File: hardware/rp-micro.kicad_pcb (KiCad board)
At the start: 2 copper layers, 17.8 x 33 mm, 46 parts, among them J1 USB_C_Receptacle_USB2.0, J2 Conn_01x12, J3 Conn_01x12, J4 Conn_01x05, SW1 BOOT, SW2 RESET, U1 RT9013-33GB, U2 W25Q16JVUXIQ, U3 RP2040, Y1 12MHz

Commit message: Update
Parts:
- removed the C1 at (144.9, 75.9)
- removed the C4 at (137.2, 66.3)
- removed the R1 at (142.6, 72.1)
- removed the R10 at (143.6, 84.6)
- removed the R6 at (141.1, 72.1)
- removed the R9 at (143.6, 85.6)
- added C15: 0.1uF, Capacitor_SMD:C_0402_1005Metric, F.Cu at (144.9, 75.9)
- added R5: 27, Resistor_SMD:R_0402_1005Metric, F.Cu at (141.1, 72.1)
- added TP2: TestPoint, TestPoint:TestPoint_Pad_D1.0mm, B.Cu at (140.7, 85.0)
- added TP3: TestPoint, TestPoint:TestPoint_Pad_D1.0mm, B.Cu at (138.7, 85.0)
- C16: renamed from C17; value 2.2uF -> 1uF
- C4: renamed from C6; value 15pF -> 20pF
- C5: renamed from C7; value 15pF -> 20pF
- C8: renamed from C10; value 2.2uF -> 1uF
- Y1: footprint Crystal:Crystal_SMD_2520-4Pin_2.5x2.0mm -> Crystal:Crystal_SMD_3225-4Pin_3.2x2.5mm
- moved kibuzzard-6360A6AE 5.50 mm to (137.7, 80.8)
- moved C4 3.94 mm to (134.0, 86.6)
- moved C13 2.54 mm to (140.1, 74.0)
- moved C16 2.54 mm to (142.6, 74.0)
- moved C10 2.33 mm to (141.7, 86.4), turned to 0 degrees
- moved C5 1.94 mm to (139.8, 86.4)
- moved C3 1.52 mm to (136.7, 66.3)
- moved R8 1.40 mm to (139.3, 84.8), turned to 90 degrees
- moved Y1 1.30 mm to (136.7, 85.9), turned to 180 degrees
- moved C6 1.15 mm to (141.7, 85.3), turned to 0 degrees
- moved R9 1.15 mm to (143.8, 85.5), turned to 90 degrees
- renumbered C2 to C1, C12 to C10, C13 to C11, C14 to C12, C15 to C13, C16 to C14, C3 to C2, C5 to C3, C8 to C6, C9 to C7, C11 to C9, R2 to R1, R13 to R10, R3 to R2, R5 to R3, R7 to R6, R8 to R7, R11 to R8, R12 to R9
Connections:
- net 16_SDA renamed 16
- net 17_SCL renamed 17
- J1 pad A6: Net-(J1-PadA6) -> USB_D+
- J1 pad A7: Net-(J1-PadA7) -> USB_D-
- J1 pad B6: Net-(J1-PadA6) -> USB_D+
- J1 pad B7: Net-(J1-PadA7) -> USB_D-
- J1 pad S1: unconnected-(J1-PadS1) -> GND
- J4 pad 1: SWCLK -> 10
- J4 pad 2: SWDIO -> 11
- J4 pad 3: GND -> 12
- R4 pad 1: Net-(J1-PadA7) -> USB_D+
- R4 pad 2: USB_D- -> Net-(R4-Pad2)
- U3 pad 13: unconnected-(U3-Pad13) -> 10
- U3 pad 14: unconnected-(U3-Pad14) -> 11
- U3 pad 15: unconnected-(U3-Pad15) -> 12
- U3 pad 43: Net-(C1-Pad1) -> +3V3
- U3 pad 46: USB_D+ -> Net-(R5-Pad2)
- U3 pad 47: USB_D- -> Net-(R4-Pad2)
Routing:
- net Net-(J1-PadA6): track 11.6 -> 0.00 mm
- net Net-(J1-PadA7): track 10.9 -> 0.00 mm, vias 2 -> 0
- net 11: track 0.00 -> 9.50 mm, vias 0 -> 1
- net GND: track 66.3 -> 57.2 mm, vias 35 -> 27
- net 10: track 0.00 -> 8.71 mm, vias 0 -> 1
- net +3V3: track 76.7 -> 68.9 mm, vias 11 -> 8
- net 12: track 0.00 -> 7.39 mm, vias 0 -> 1
- net USB_D+: track 3.61 -> 10.9 mm
- net USB_D-: track 3.82 -> 10.9 mm, vias 0 -> 2
- net Net-(C1-Pad1): track 6.17 -> 0.00 mm
- net Net-(R4-Pad2): track 0.00 -> 3.82 mm
- net Net-(R5-Pad2): track 0.00 -> 3.61 mm
- net Net-(C4-Pad2): track 6.19 -> 7.76 mm
- net SWDIO: track 8.85 -> 10.0 mm, vias 0 -> 1
- net 16: track 9.02 -> 10.0 mm
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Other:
- board text added: "10"
- board text added: "11"
- board text added: "12"
- board text removed: "SWC"
- board text removed: "SWD"

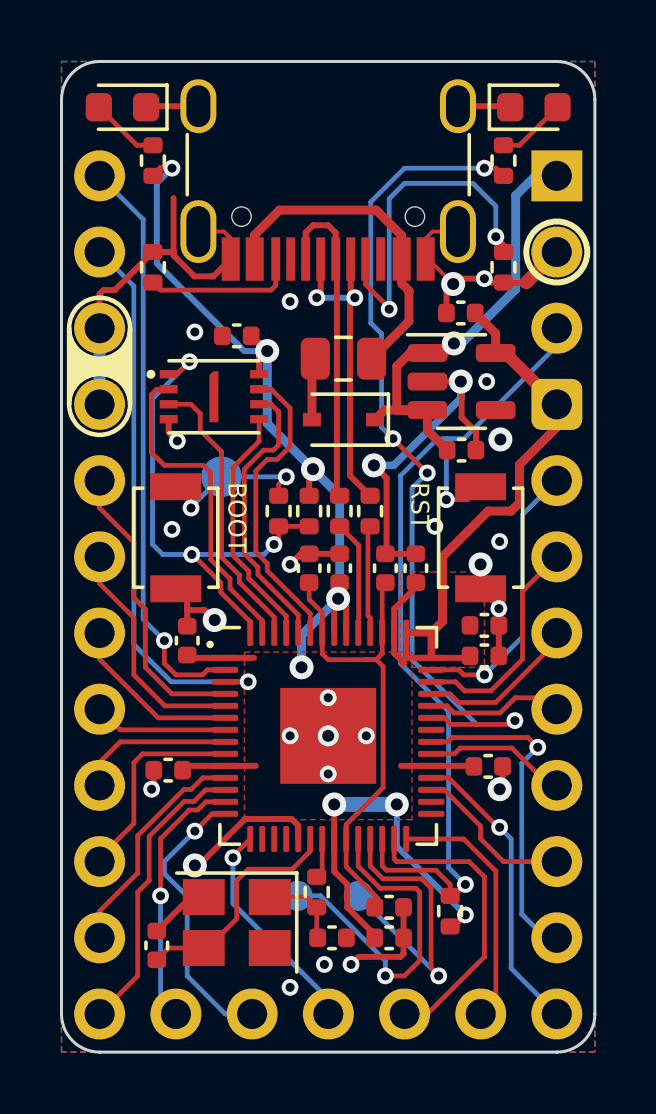
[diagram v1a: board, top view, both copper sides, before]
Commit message: Replace flash to W25Q64JVXGIQ
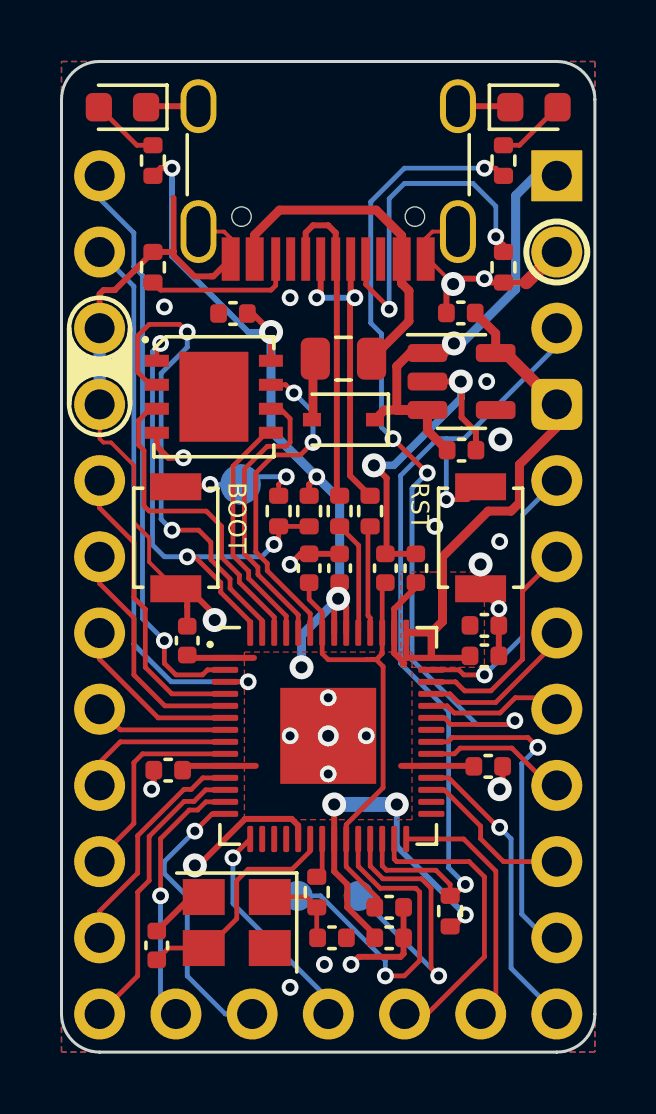
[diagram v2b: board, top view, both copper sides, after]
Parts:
- U2: value W25Q16JVUXIQ -> W25Q64JVXGIQ; footprint rp-micro:USON-8 (2x3mm) -> rp-micro:XSON-8 (4x4mm)
- moved C3 0.75 mm to (136.5, 65.5)
- moved TP1 0.68 mm to (136.8, 71.2)
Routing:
- net GND: track 57.2 -> 65.0 mm, vias 27 -> 26
- net QSPI_1: track 10.9 -> 16.2 mm, vias 0 -> 2
- net QSPI_2: track 9.51 -> 10.8 mm
- net QSPI_3: track 10.2 -> 11.2 mm, vias 0 -> 2
- net +3V3: track 68.9 -> 68.2 mm
- net BOOT: track 5.28 -> 4.56 mm

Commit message: Improve 3v3 route
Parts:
- TP2: value TestPoint -> SWDIO
- TP3: value TestPoint -> SWCLK
- turned U2 to 0 degrees
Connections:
- U1 pad 4: (no net) -> unconnected-(U1-Pad4)
- U2 pad 9: (no net) -> unconnected-(U2-Pad9)
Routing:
- net +1V1: track 16.3 -> 21.5 mm, vias 0 -> 2
- net +3V3: track 68.2 -> 66.9 mm, vias 8 -> 7
